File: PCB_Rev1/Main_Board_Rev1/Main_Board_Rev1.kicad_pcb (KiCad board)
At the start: 4 copper layers, 152.4 x 152.4 mm, 83 parts, among them IC1 LT8648SEV#PBF, J1 PRT-14017, J10 B4B-PH-K-S, J11 532610771, J12 532610771, J13 532610771, J2 Conn_01x04_Socket, J3 691137710002, J4 Conn_01x02_Pin, J5 XT60PW-M, J6 Conn_01x02_Pin, J7 Conn_01x02_Pin, J8 Conn_01x02_Pin, J9 B4B-PH-K-S, Q1 AO3400A, Q2 AO3400A, Q3 AO3400A, Q4 IRFHM9331TRPBF, U1 AZ1117IH-3.3TRG1, U2 L298N, X1 B2P-VH, X2 B2P-VH

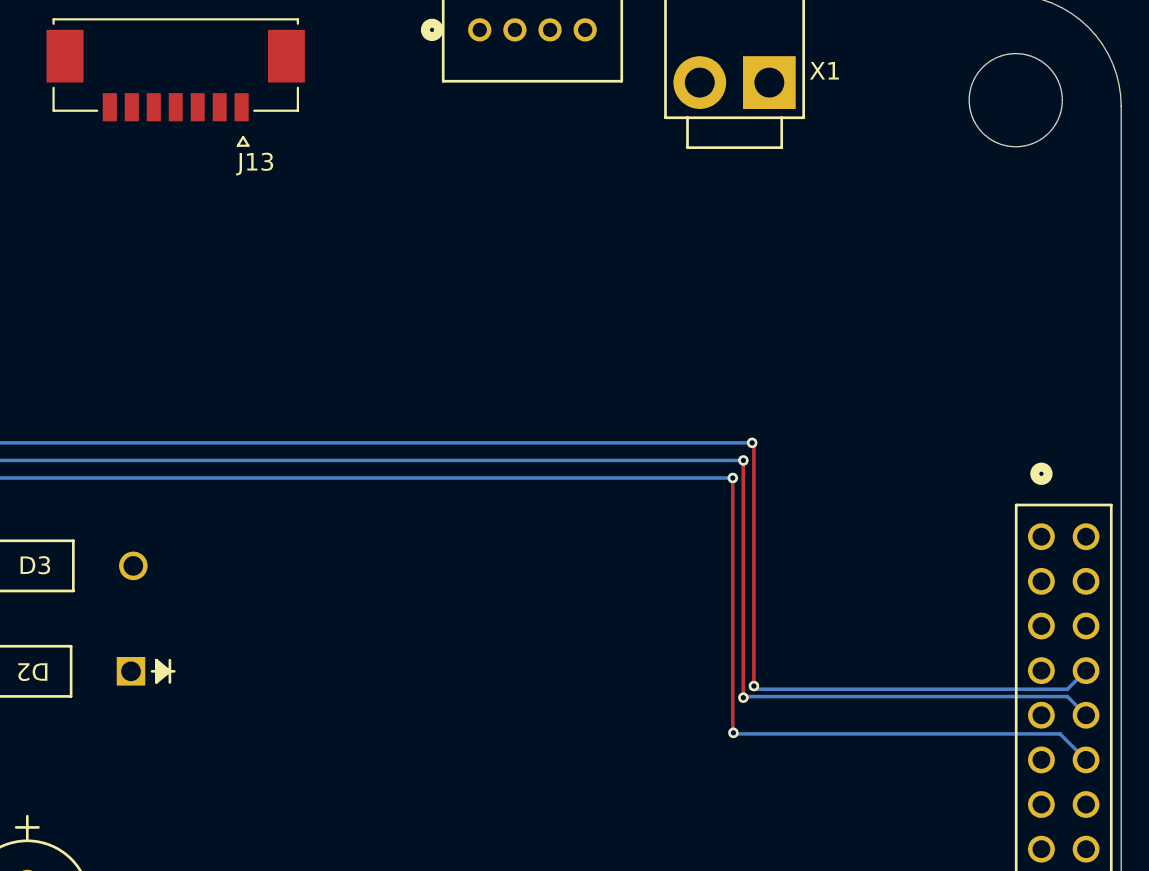
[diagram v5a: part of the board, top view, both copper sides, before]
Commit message: J12 connector routing
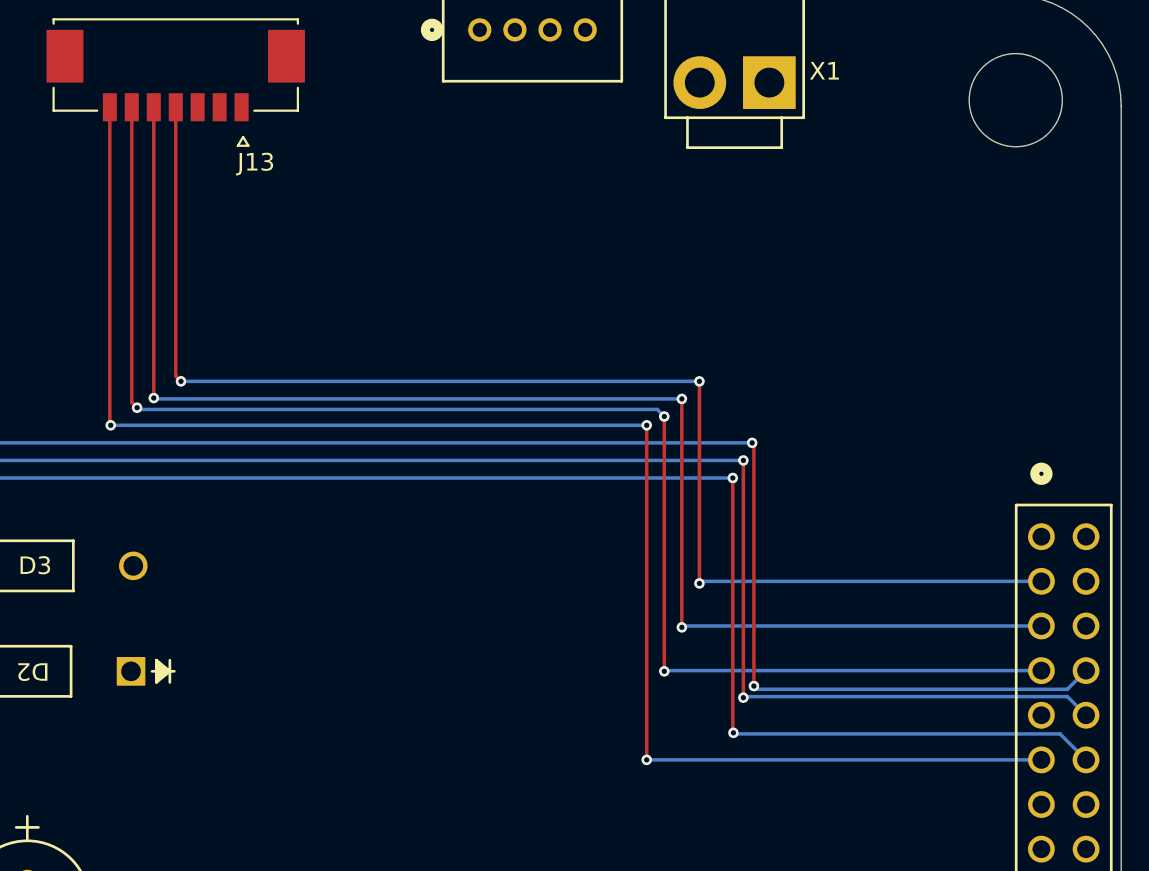
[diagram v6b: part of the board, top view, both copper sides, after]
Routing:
- net GPIO0: track 0.00 -> 90.3 mm, vias 0 -> 3
- net GPIO7: track 0.00 -> 83.4 mm, vias 0 -> 3
- net GPIO9: track 0.00 -> 80.2 mm, vias 0 -> 3
- net GPIO8: track 0.00 -> 76.2 mm, vias 0 -> 3

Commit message: Routing
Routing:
- net GPIO12: track 127.5 -> 143.6 mm
- net GPIO13: track 144.2 -> 144.0 mm, vias 4 -> 3
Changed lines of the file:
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@@
 	)
 	(segment
-		(start 149.4 72.6)
+		(start 149.4 73)
 		(end 149.4 84.885421)
 		(width 0.2)
@@
 	)
 	(via
-		(at 149.5 72.5)
+		(at 149.4 73)
 		(size 0.6)
 		(drill 0.3)
@@
 		(drill 0.3)
 		(layers "F.Cu" "B.Cu")
+		(net 61)
+	)
+	(segment
+		(start 149.5 73)
+		(end 149.8 72.7)
+		(width 0.2)
+		(layer "B.Cu")
+		(net 61)
+	)
+	(segment
+		(start 149.8 72.7)
+		(end 165.96 72.7)
+		(width 0.2)
+		(layer "B.Cu")
+		(net 61)
+	)
+	(segment
+		(start 149.4 73)
+		(end 149.5 73)
+		(width 0.2)
+		(layer "B.Cu")
 		(net 61)
 	)
@@
 	)
 	(segment
-		(start 149.5 72.5)
-		(end 149.4 72.6)
-		(width 0.2)
-		(layer "B.Cu")
-		(net 61)
-	)
-	(segment
 		(start 115.45 25.4)
 		(end 115.45 41.95)
@@
 	)
 	(segment
-		(start 150 75)
-		(end 150 85.5)
-		(width 0.2)
-		(layer "F.Cu")
-		(net 75)
-	)
-	(segment
 		(start 92.45 25.4)
 		(end 92.45 85.45)
@@
 		(net 75)
 	)
+	(segment
+		(start 150 75.5)
+		(end 150 85.5)
+		(width 0.2)
+		(layer "F.Cu")
+		(net 75)
+	)
 	(via
 		(at 150 85.5)
@@
 	)
 	(via
-		(at 150 75)
+		(at 150 75.5)
 		(size 0.6)
 		(drill 0.3)
@@
 		(drill 0.3)
 		(layers "F.Cu" "B.Cu")
-		(net 75)
-	)
-	(via
-		(at 163 75)
-		(size 0.6)
-		(drill 0.3)
-		(layers "F.Cu" "B.Cu")
-		(net 75)
-	)
-	(segment
-		(start 150 75)
-		(end 163 75)
-		(width 0.2)
-		(layer "B.Cu")
-		(net 75)
-	)
-	(segment
-		(start 164 75)
-		(end 165.72 75)
-		(width 0.2)
-		(layer "B.Cu")
 		(net 75)
 	)
@@
 	)
 	(segment
+		(start 150.26 75.24)
+		(end 165.96 75.24)
+		(width 0.2)
+		(layer "B.Cu")
+		(net 75)
+	)
+	(segment
+		(start 150 75.5)
+		(end 150.26 75.24)
+		(width 0.2)
+		(layer "B.Cu")
+		(net 75)
+	)
+	(segment
 		(start 165.72 75)
 		(end 165.96 75.24)
 		(width 0.2)
 		(layer "B.Cu")
-		(net 75)
-	)
-	(segment
-		(start 163 75)
-		(end 164 75)
-		(width 0.2)
-		(layer "B.Cu")

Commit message: Routing
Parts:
- moved Q1 1.84 mm to (33.0, 125.0)
- moved Q2 1.81 mm to (33.0, 115.0)
- moved Q3 1.50 mm to (40.8, 120.0)
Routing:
- net RGB_Red_Control: track 0.00 -> 183.8 mm, vias 0 -> 6
- net RGB_Green_Control: track 0.00 -> 172.0 mm, vias 0 -> 6
- net RGB_Blue_Control: track 0.00 -> 166.5 mm, vias 0 -> 4
- net GPIO3: track 0.00 -> 113.0 mm, vias 0 -> 4
- net GPIO2: track 0.00 -> 109.2 mm, vias 0 -> 3
- net /CSTAR-Drive/OUT1_MOTOR_2: track 0.00 -> 101.9 mm, vias 0 -> 8
- net Net-(J2-Pin_4): track 0.00 -> 28.9 mm, vias 0 -> 5
- net Net-(J2-Pin_2): track 0.00 -> 27.9 mm, vias 0 -> 6
- net GPIO12: track 143.6 -> 119.3 mm, vias 5 -> 6
- net GPIO13: track 144.0 -> 124.0 mm, vias 3 -> 6
- net Net-(J2-Pin_3): track 0.00 -> 19.4 mm, vias 0 -> 3
- net /CSTAR-Drive/OUT2_MOTOR_1: track 0.00 -> 6.11 mm
- net RXD_LIDAR: track 130.2 -> 130.9 mm, vias 3 -> 4
- net GPIO7: track 83.4 -> 83.9 mm, vias 3 -> 4
- net GPIO8: track 76.2 -> 76.5 mm, vias 3 -> 4
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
